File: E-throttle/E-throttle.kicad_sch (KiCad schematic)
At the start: 50 parts, among them IC1 BTS441TG, J1 Micro_SD_Card_Det1, J3 Conn_01x11, J4 Conn_01x11, J5 776087-1, J6 Conn_01x15, J7 Conn_01x15, Q1 NMOS, SW1 SW_Push, U1 74HC123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

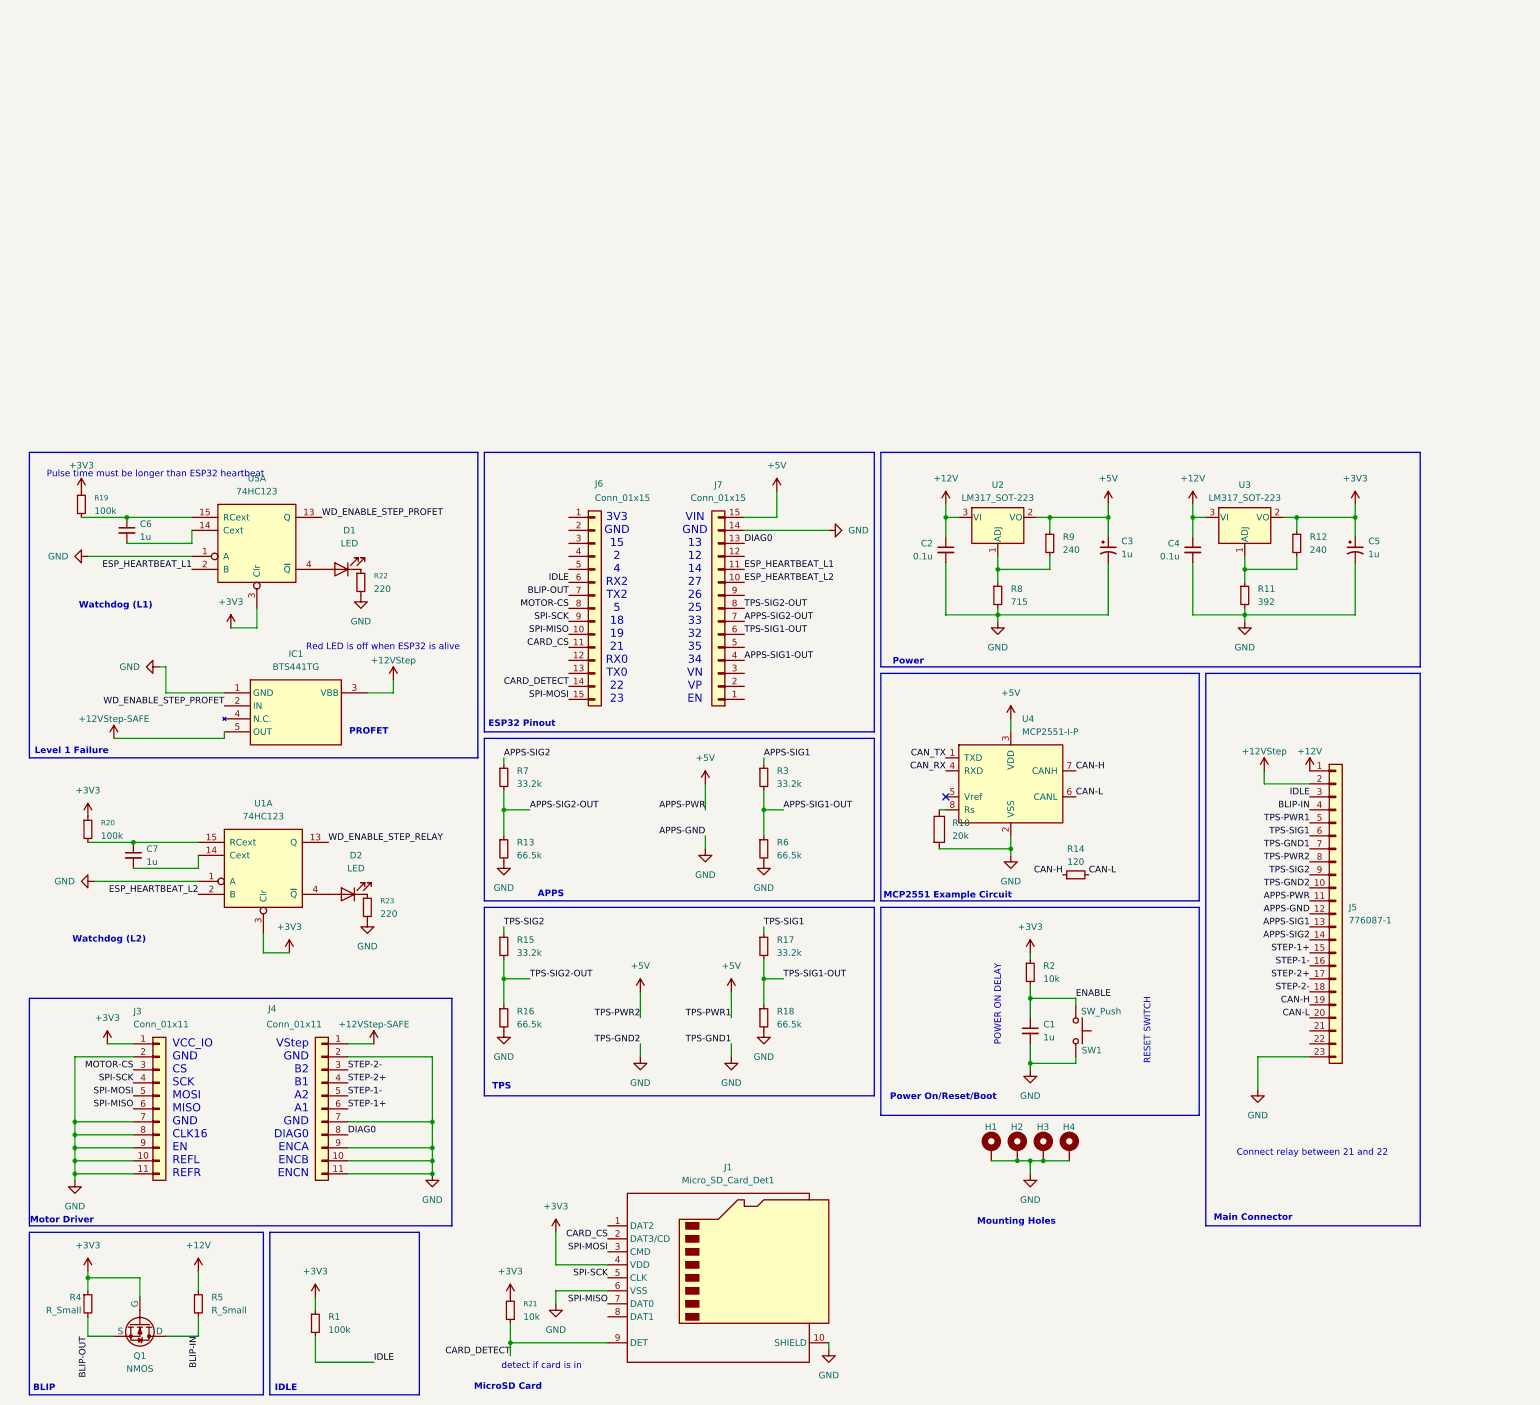
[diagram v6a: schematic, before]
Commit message: Added relay, added all footprints to schematic
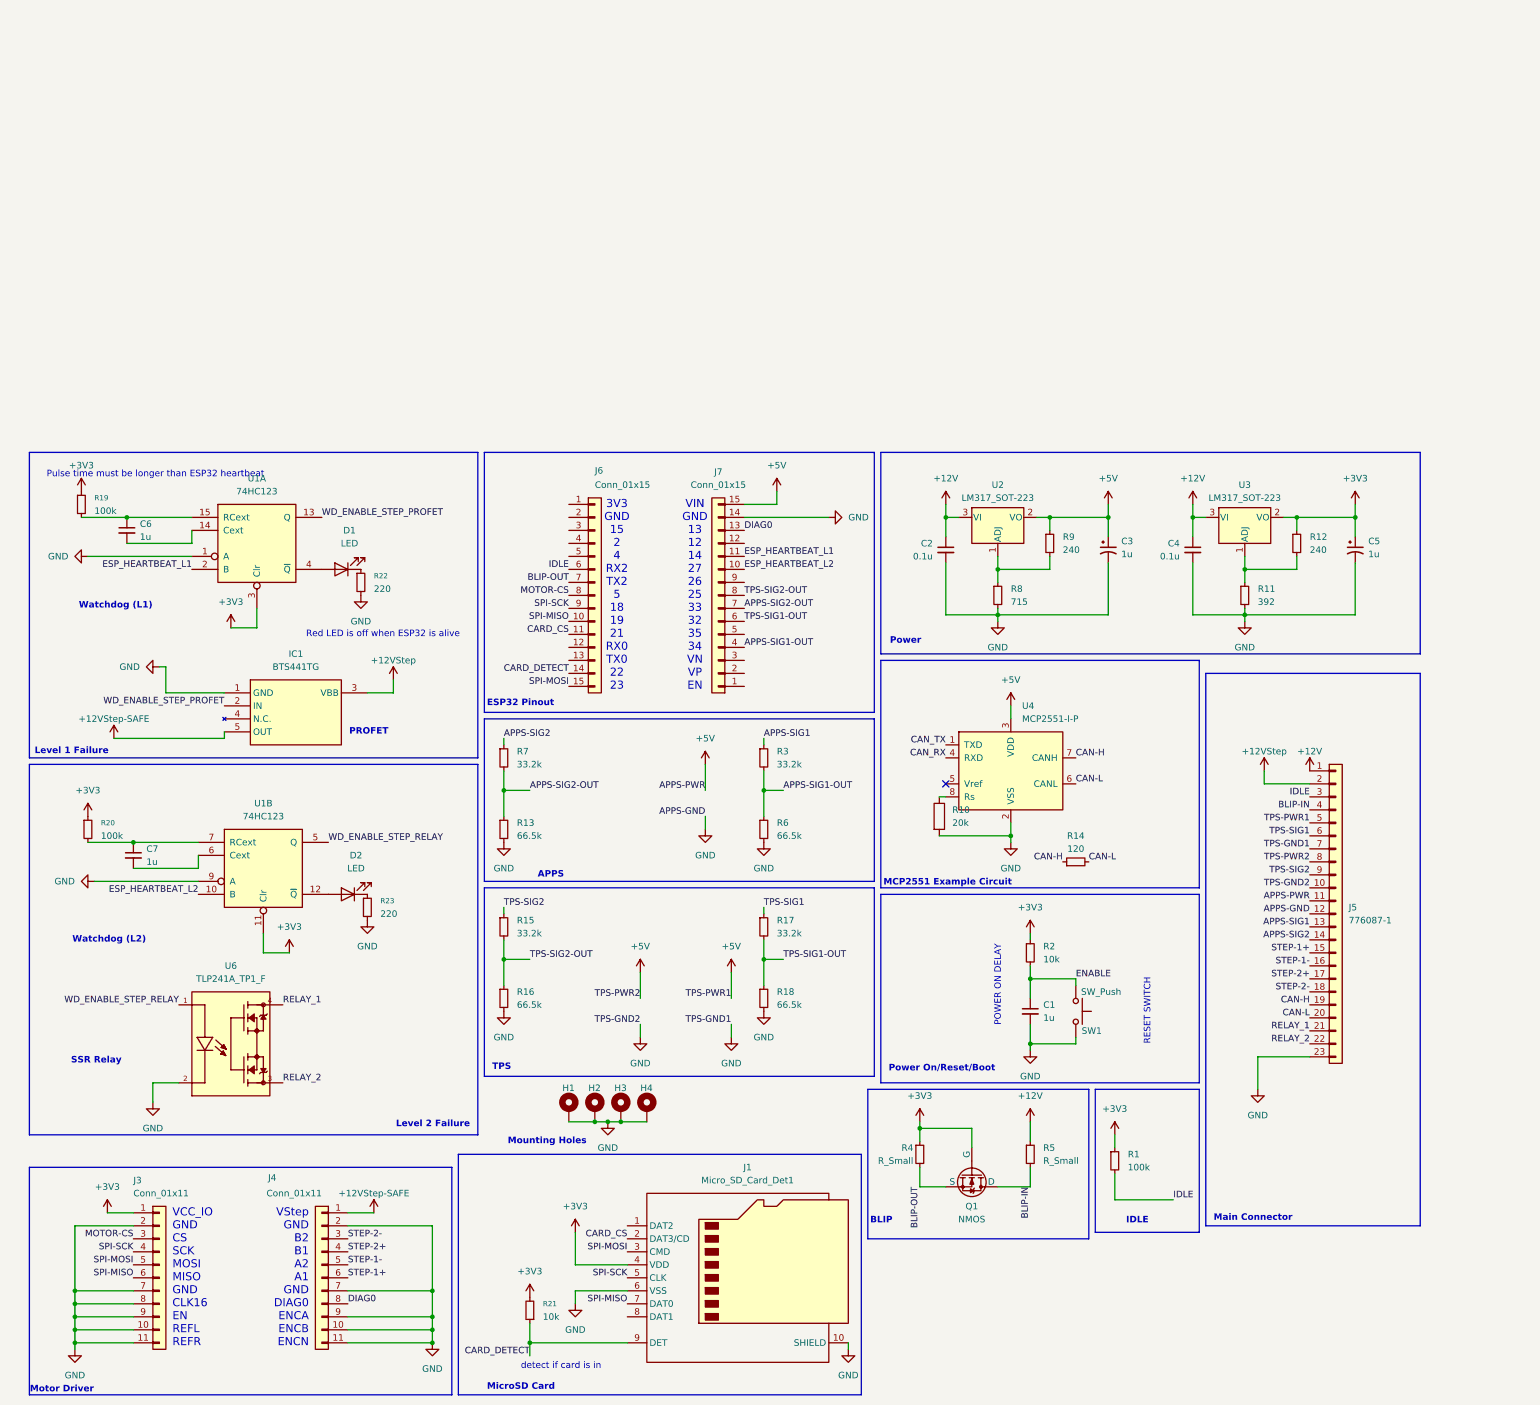
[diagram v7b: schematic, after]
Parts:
- added U6: TLP241A_TP1_F, TLP241A_TP1_F:SOIC254P1000X425-4N, symbol TLP241A_TP1_F:TLP241A_TP1_F
- D1, D2: footprint (none) -> LED_THT:LED_D5.0mm
- IC1: footprint BTS441TG -> BTS441TG_KiCad:BTS441TG
- J1: footprint (none) -> Connector_Card:microSD_HC_Hirose_DM3AT-SF-PEJM5
- R21, R22, R23: footprint (none) -> Resistor_THT:R_Axial_DIN0207_L6.3mm_D2.5mm_P10.16mm_Horizontal
- U1: renamed from U5; footprint (none) -> Package_SO:SOIC-16_3.9x9.9mm_P1.27mm
- U1: footprint (none) -> Package_SO:SOIC-16_3.9x9.9mm_P1.27mm
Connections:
- net +3V3: now also U1.11 (Clr); no longer U1.3 (Clr)
- net ESP_HEARTBEAT_L2: now also U1.10 (B); no longer U1.2 (B)
- net GND: now also U1.9 (A), U6.2; no longer U1.1 (A)
- net WD_ENABLE_STEP_RELAY: now also U1.5 (Q), U6.1; no longer U1.13 (Q)
- net at D2.2 (A): now also U1.12 (~{Q}); no longer U1.4 (~{Q})
- net at C7.1, R20.2: now also U1.7 (RCext); no longer U1.15 (RCext)
- net at C7.2: now also U1.6 (Cext); no longer U1.14 (Cext)
- net RELAY_1: now reaches J5.21 (Pin_21)
- net RELAY_1: now also U6.4
- net RELAY_2: now reaches J5.22 (Pin_22)
- net RELAY_2: now also U6.3
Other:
- note added: "Level 2 Failure"
- note added: "SSR Relay"
- note removed: "Connect relay between 21 and 22"
- moved on the sheet: C1, H1, H2, H3, H4, J1, J3, J4, J6, J7, Q1, R1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

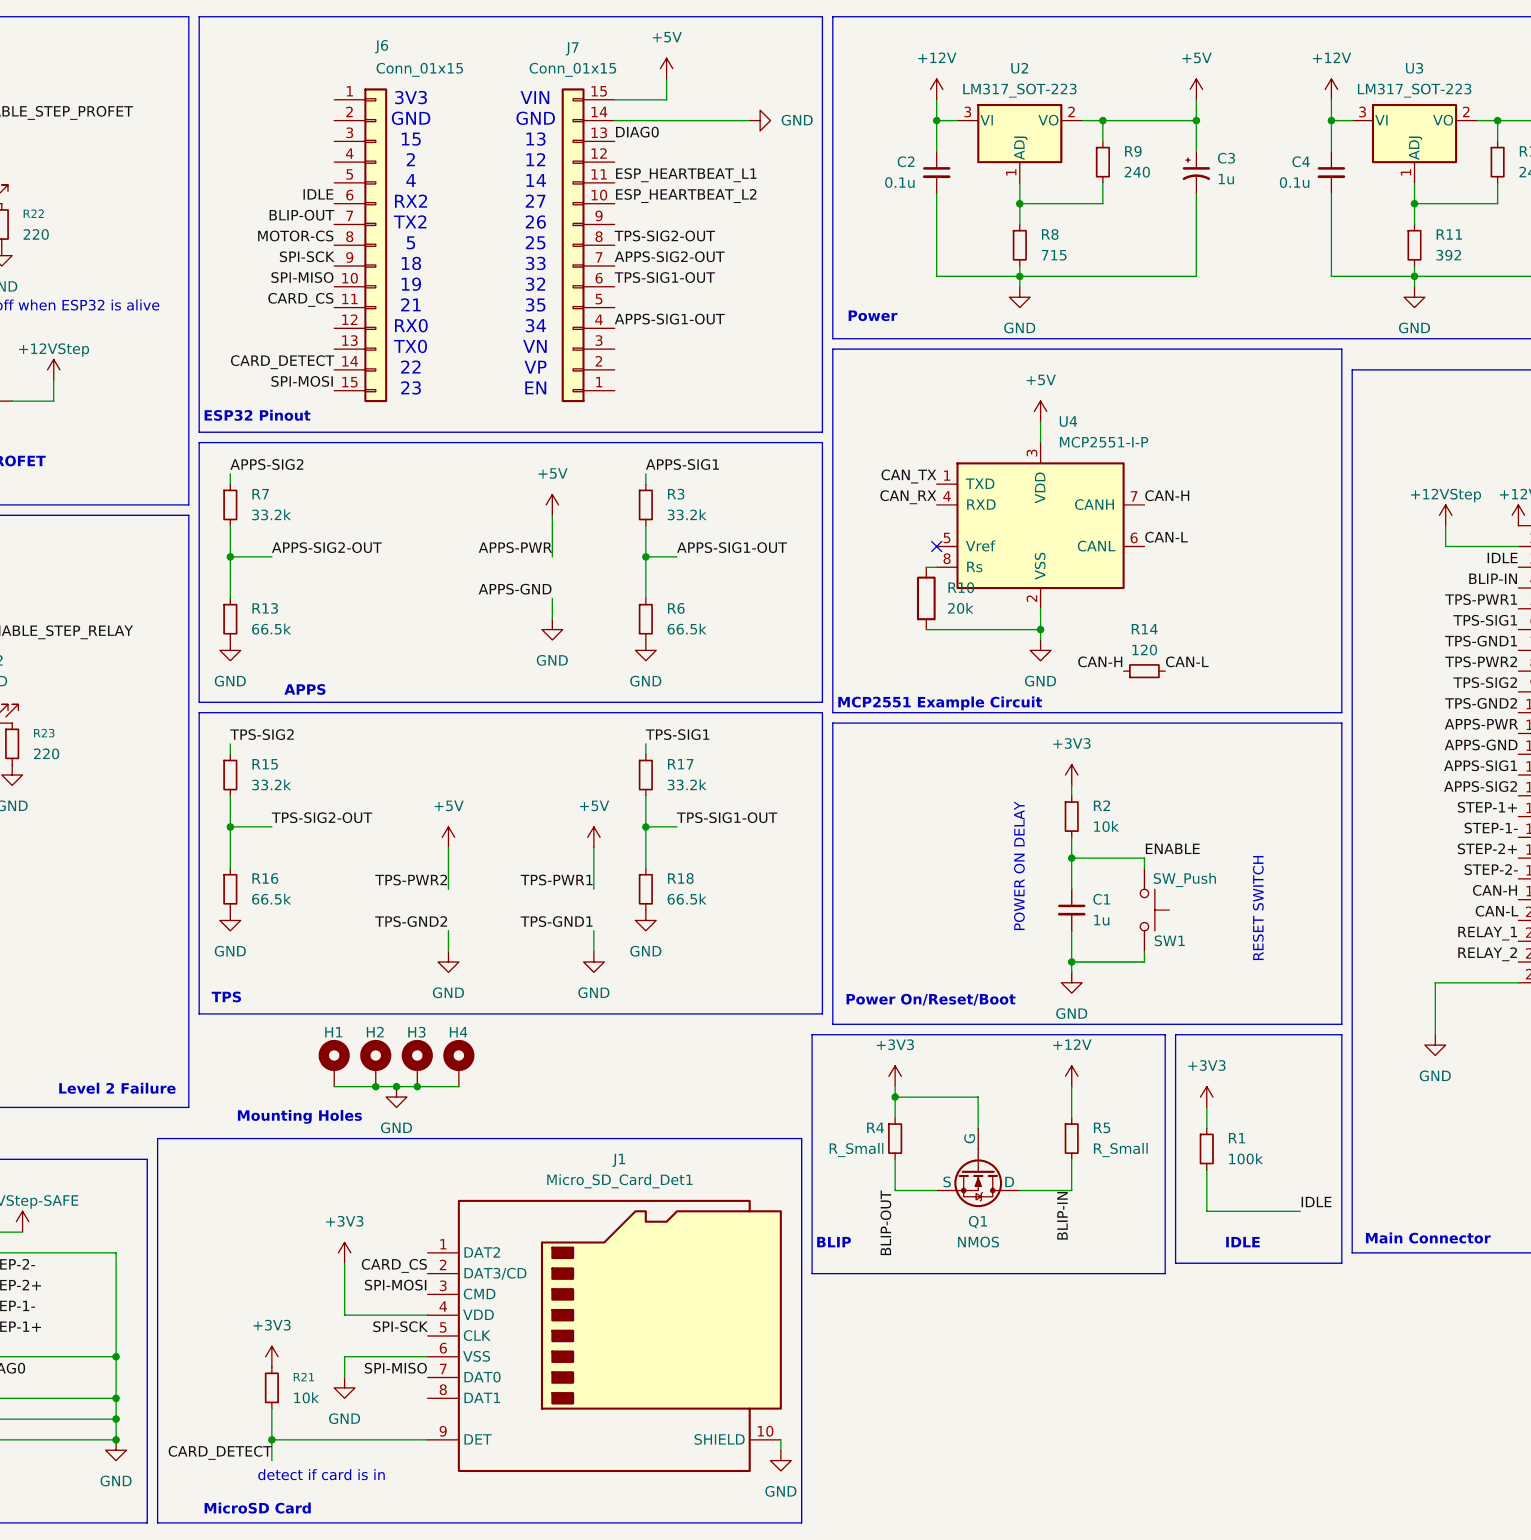
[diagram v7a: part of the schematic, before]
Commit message: Initial PCB Layout edit
- Added ESP32 Dev Board footprint
- Expanded PCB layout edges
- Added all components in new layout
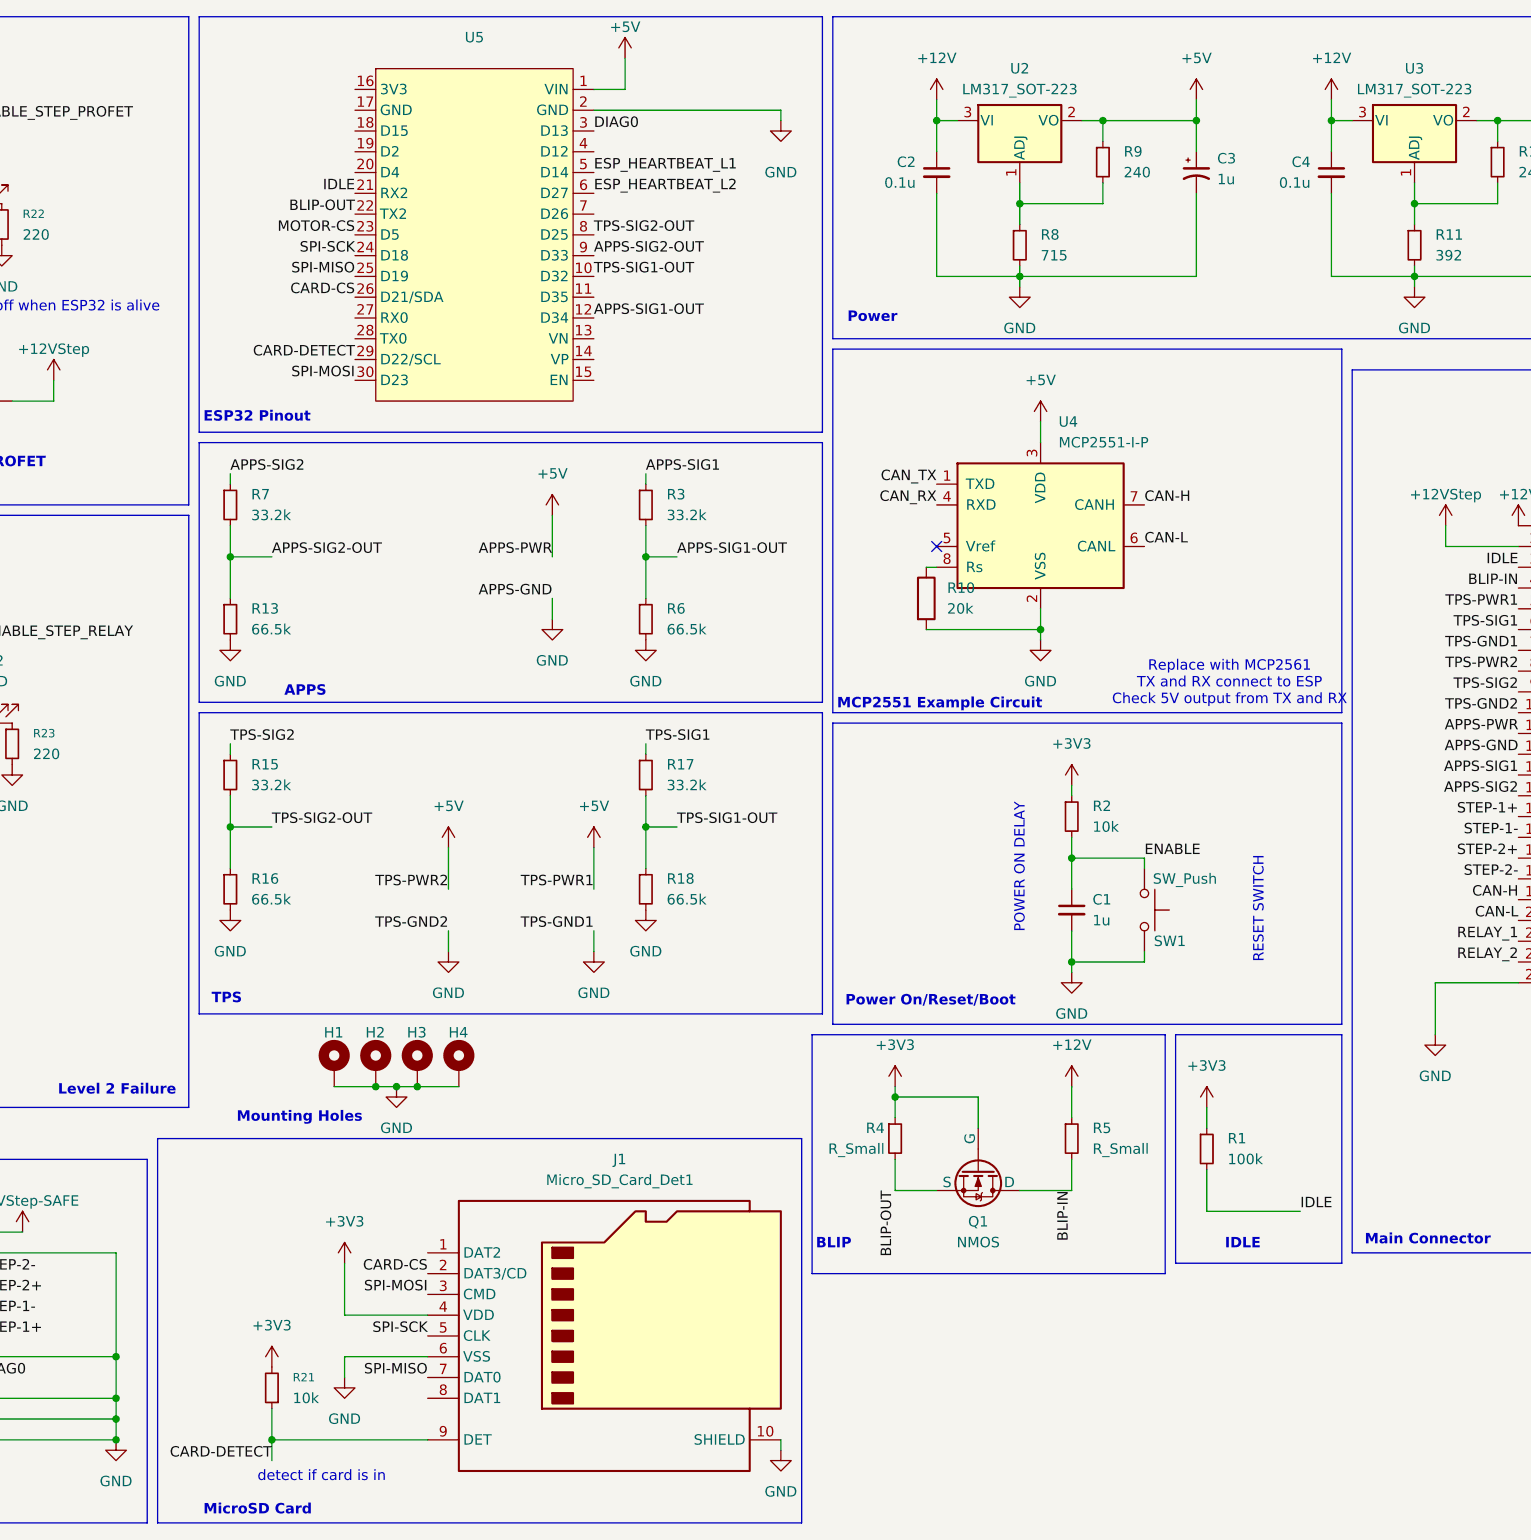
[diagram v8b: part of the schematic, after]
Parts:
- removed J6, J7: Conn_01x15, Connector_PinSocket_2.54mm:PinSocket_1x15_P2.54mm_Vertical, symbol Connector_Generic:Conn_01x15
- removed R14: 120, Resistor_THT:R_Axial_DIN0207_L6.3mm_D2.5mm_P10.16mm_Horizontal, symbol Device:R_Small
- added U5: ~, FBR_Footprints_additional:ESP32_30pin, symbol FBR_Symbols_additional:ESP32-30Pin-BOB-FBR26
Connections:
- net +5V: now also U5.1 (VIN)
- net APPS-SIG1-OUT: now also U5.12 (D34)
- net APPS-SIG2-OUT: now also U5.9 (D33)
- net BLIP-OUT: now also U5.22 (TX2)
- net DIAG0: now also U5.3 (D13)
- net ESP_HEARTBEAT_L1: now also U5.5 (D14)
- net ESP_HEARTBEAT_L2: now also U5.6 (D27)
- net GND: now also U5.2 (GND)
- net IDLE: now also U5.21 (RX2)
- net MOTOR-CS: now also U5.23 (D5)
- net SPI-MISO: now also U5.25 (D19)
- net SPI-MOSI: now also U5.30 (D23)
- net SPI-SCK: now also U5.24 (D18)
- net TPS-SIG1-OUT: now also U5.10 (D32)
- net TPS-SIG2-OUT: now also U5.8 (D25)
- net CARD_CS renamed CARD-CS
- net CARD-CS: now also U5.26 (D21/SDA)
- net CARD_DETECT renamed CARD-DETECT
- net CARD-DETECT: now also U5.29 (D22/SCL)
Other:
- note added: "Replace with MCP2561 TX and RX connect to ESP Check 5V output from TX and RX"
- note removed: "3V3 GND 15 2 4 RX2 TX2 5 18 19 21 RX0 TX0 22 23"
- note removed: "VIN GND 13 12 14 27 26 25 33 32 35 34 VN VP EN"
